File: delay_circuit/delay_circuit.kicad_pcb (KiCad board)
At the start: 2 copper layers, 97.5 x 139 mm, 26 parts, among them J1 IN 12V AC, J2 OUT 230V AC, J3 IN 230V AC, J4 From Trfo Output, J5 OUT 5V CC, J6 To Power Ampli Power IN, J7 From Ampli Output, J8 OUT 12V CC, J9 To Speakers, K1 SANYOU_SRD_Form_C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

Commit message: Fixed issues in source
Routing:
- net 0: track 0.42 -> 95.9 mm, vias 0 -> 2
- net Net-(D2-A): track 81.2 -> 82.9 mm
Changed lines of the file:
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@@
 		(legacy_teardrops no)
 	)
-	(paper "A4")
+	(paper "A4" portrait)
 	(layers
 		(0 "F.Cu" signal)
@@
 	)
 	(segment
+		(start 85 115)
+		(end 85 130)
+		(width 1.75)
+		(layer "F.Cu")
+		(net 3)
+	)
+	(via
+		(at 85 130)
+		(size 2.5)
+		(drill 0.8)
+		(layers "F.Cu" "B.Cu")
+		(net 3)
+	)
+	(via
+		(at 85 115)
+		(size 2.5)
+		(drill 0.8)
+		(layers "F.Cu" "B.Cu")
+		(net 3)
+	)
+	(segment
+		(start 107.5 125)
+		(end 103 129.5)
+		(width 1.75)
+		(layer "B.Cu")
+		(net 3)
+	)
+	(segment
+		(start 85 130)
+		(end 85 132.5)
+		(width 1.75)
+		(layer "B.Cu")
+		(net 3)
+	)
+	(segment
+		(start 103.294888 136)
+		(end 103.294888 129.794888)
+		(width 1.75)
+		(layer "B.Cu")
+		(net 3)
+	)
+	(segment
+		(start 102 96.88)
+		(end 102 107)
+		(width 1.75)
+		(layer "B.Cu")
+		(net 3)
+	)
+	(segment
+		(start 100 140)
+		(end 102.5 140)
+		(width 1.75)
+		(layer "B.Cu")
+		(net 3)
+	)
+	(segment
+		(start 102.5 140)
+		(end 103.294888 139.205112)
+		(width 1.75)
+		(layer "B.Cu")
+		(net 3)
+	)
+	(segment
 		(start 103.294888 129.794888)
 		(end 103 129.5)
@@
 	)
 	(segment
+		(start 95 135)
+		(end 100 140)
+		(width 1.75)
+		(layer "B.Cu")
+		(net 3)
+	)
+	(segment
+		(start 77.5775 108.5375)
+		(end 78.5375 108.5375)
+		(width 2)
+		(layer "B.Cu")
+		(net 3)
+	)
+	(segment
+		(start 85 132.5)
+		(end 87.5 135)
+		(width 1.75)
+		(layer "B.Cu")
+		(net 3)
+	)
+	(segment
+		(start 102 107)
+		(end 107.5 112.5)
+		(width 1.75)
+		(layer "B.Cu")
+		(net 3)
+	)
+	(segment
+		(start 107.5 112.5)
+		(end 107.5 125)
+		(width 1.75)
+		(layer "B.Cu")
+		(net 3)
+	)
+	(segment
+		(start 78.5375 108.5375)
+		(end 85 115)
+		(width 2)
+		(layer "B.Cu")
+		(net 3)
+	)
+	(segment
+		(start 103.294888 139.205112)
+		(end 103.294888 136)
+		(width 1.75)
+		(layer "B.Cu")
+		(net 3)
+	)
+	(segment
+		(start 87.5 135)
+		(end 95 135)
+		(width 1.75)
+		(layer "B.Cu")
+		(net 3)
+	)
+	(segment
 		(start 42 32)
 		(end 41.5 32.5)
@@
 	)
 	(segment
-		(start 56 102)
+		(start 55 102)
 		(end 63.5 102)
 		(width 2)
@@
 	)
 	(via
-		(at 56 102)
+		(at 55 102)
 		(size 2.5)
 		(drill 0.8)
@@
 	)
 	(segment
-		(start 49.5 102)
-		(end 56 102)
-		(width 1.2)
+		(start 68.25 101.75)
+		(end 71.5 105)
+		(width 2)
 		(layer "B.Cu")
 		(net 7)
@@
 		(start 67.55 96.05)
 		(end 67.55 100.95)
-		(width 1.2)
+		(width 2)
 		(layer "B.Cu")
 		(net 7)
@@
 	(segment
 		(start 47.05 99.45)
-		(end 47 99.5)
-		(width 1.2)
+		(end 47.05 96.05)
+		(width 2)
 		(layer "B.Cu")
 		(net 7)
@@
 		(start 68 102)
 		(end 68.25 101.75)
-		(width 1.2)
+		(width 2)
 		(layer "B.Cu")
 		(net 7)
@@
 	)
 	(segment
-		(start 99.58 88.4)
-		(end 91.1 96.88)
-		(width 1.2)
-		(layer "B.Cu")
-		(net 7)
-	)
-	(segment
 		(start 67.55 100.95)
 		(end 67.5 101)
@@
 		(start 67.5 101)
 		(end 68.25 101.75)
-		(width 1.2)
+		(width 2)
 		(layer "B.Cu")
 		(net 7)
@@
 		(start 89 107.5)
 		(end 89 103.5)
+		(width 2)
+		(layer "B.Cu")
+		(net 7)
+	)
+	(segment
+		(start 91.1 96.88)
+		(end 91.1 94.94)
 		(width 1.2)
 		(layer "B.Cu")
@@
 		(start 63.5 102)
 		(end 68 102)
-		(width 1.2)
+		(width 2)
 		(layer "B.Cu")
 		(net 7)
 	)
 	(segment
-		(start 69.5 103)
-		(end 88.5 103)
-		(width 1.2)
+		(start 49.5 102)
+		(end 47 99.5)
+		(width 2)
 		(layer "B.Cu")
 		(net 7)
 	)
 	(segment
-		(start 68.25 101.75)
-		(end 69.5 103)
-		(width 1.2)
+		(start 91.1 94.94)
+		(end 99.58 86.46)
+		(width 2)
 		(layer "B.Cu")
 		(net 7)
@@
 	)
 	(segment
-		(start 99.58 86.46)
-		(end 99.58 88.4)
+		(start 47 99.5)
+		(end 47.05 99.45)
 		(width 1.2)
 		(layer "B.Cu")
@@
 	)
 	(segment
-		(start 47 99.5)
+		(start 86.5 105)
+		(end 88.5 103)
+		(width 2)
+		(layer "B.Cu")
+		(net 7)
+	)
+	(segment
+		(start 55 102)
 		(end 49.5 102)
-		(width 1.2)
+		(width 2)
 		(layer "B.Cu")
 		(net 7)
@@
 		(start 89 100)
 		(end 91.1 97.9)
-		(width 1.2)
+		(width 2)
 		(layer "B.Cu")
 		(net 7)
 	)
 	(segment
-		(start 47.05 96.05)
-		(end 47.05 99.45)
-		(width 1.2)
+		(start 71.5 105)
+		(end 86.5 105)
+		(width 2)
 		(layer "B.Cu")
 		(net 7)
@@
 		(start 89 103.5)
 		(end 89 100)
-		(width 1.2)
+		(width 2)
 		(layer "B.Cu")
 		(net 7)
@@
 		(start 79.55 96.05)
 		(end 79.55 93.05)
-		(width 1.2)
+		(width 2)
 		(layer "B.Cu")
 		(net 8)
@@
 		(start 60.5375 123.5375)
 		(end 59 122)
-		(width 1.2)
+		(width 2)
 		(layer "B.Cu")
 		(net 8)
@@
 		(start 59.05 93.95)
 		(end 59.05 96.05)
-		(width 1.2)
+		(width 2)
 		(layer "B.Cu")
 		(net 8)
@@
 		(start 78.5 92)
 		(end 61 92)
-		(width 1.2)
+		(width 2)
 		(layer "B.Cu")
 		(net 8)
@@
 		(start 86.14 86.46)
 		(end 79.55 93.05)
-		(width 1.2)
+		(width 2)
 		(layer "B.Cu")
 		(net 8)
@@
 		(start 89.42 86.46)
 		(end 86.14 86.46)
-		(width 1.2)
+		(width 2)
 		(layer "B.Cu")
 		(net 8)
@@
 		(start 77.5775 123.5375)
 		(end 60.5375 123.5375)
-		(width 1.2)
+		(width 2)
 		(layer "B.Cu")
 		(net 8)
@@
 		(start 61 92)
 		(end 59.05 93.95)
-		(width 1.2)
+		(width 2)
 		(layer "B.Cu")
 		(net 8)
@@
 		(start 59.05 121.95)
 		(end 59.05 96.05)
-		(width 1.2)
+		(width 2)
 		(layer "B.Cu")
 		(net 8)
@@
 		(start 79.55 93.05)
 		(end 78.5 92)
-		(width 1.2)
+		(width 2)
 		(layer "B.Cu")
 		(net 8)
@@
 		(min_thickness 0.25)
 		(filled_areas_thickness no)
-		(fill yes
+		(fill
 			(thermal_gap 0.5)
 			(thermal_bridge_width 0.5)
@@
 		(min_thickness 0.25)
 		(filled_areas_thickness no)
-		(fill yes
+		(fill
 			(thermal_gap 0.5)
 			(thermal_bridge_width 0.5)
@@
 		(min_thickness 0.25)
 		(filled_areas_thickness no)
-		(fill yes
+		(fill
 			(thermal_gap 0.5)
 			(thermal_bridge_width 0.5)
@@
 		(min_thickness 0.25)
 		(filled_areas_thickness no)
-		(fill yes
+		(fill
 			(thermal_gap 0.5)
 			(thermal_bridge_width 0.5)
@@
 		(min_thickness 0.25)
 		(filled_areas_thickness no)
-		(fill yes
+		(fill
 			(thermal_gap 0.5)
 			(thermal_bridge_width 0.5)

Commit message: WIP
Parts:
- Q2: footprint Package_TO_SOT_THT:TO-3P-3_Vertical -> Package_TO_SOT_THT:TO-126-3_Vertical
- moved J5 10.1 mm to (95.0, 140.0), turned to -90 degrees
- moved Q2 9.52 mm to (92.7, 87.5)
- moved C1 7.00 mm to (73.8, 40.0)
- moved C2 7.00 mm to (62.8, 40.0)
- moved C3 7.00 mm to (100.5, 129.0)
- moved C4 7.00 mm to (41.2, 25.5)
- moved C5 7.00 mm to (62.8, 25.0)
- moved D1 7.00 mm to (42.8, 35.5)
- moved D2 7.00 mm to (89.2, 79.5)
- moved J1 7.00 mm to (28.0, 35.5)
- moved J2 7.00 mm to (27.2, 122.5)
- moved J3 7.00 mm to (27.2, 137.7)
- moved J4 7.00 mm to (27.8, 51.0)
- moved J6 7.00 mm to (27.8, 76.5)
- moved J7 7.00 mm to (27.2, 97.0)
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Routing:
- net Net-(J5-Pin_2): track 37.3 -> 43.8 mm
- net 0: track 95.9 -> 100.3 mm
- net Net-(J5-Pin_1): track 22.6 -> 18.8 mm
- net Net-(J7-Pin_4): track 110.3 -> 113.4 mm
- net Net-(Q1-E): track 21.1 -> 24.0 mm
- net OUT SP L+: track 75.0 -> 77.7 mm
- net OUT SP R+: track 72.0 -> 69.4 mm
- net 12V GND: track 150.9 -> 152.7 mm
- net Net-(D2-K): track 99.2 -> 100.5 mm
- net IN SP L+: track 71.5 -> 70.3 mm

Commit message: WIP
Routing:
- net 0: track 100.3 -> 105.3 mm
- net Net-(J2-Pin_2): track 73.8 -> 71.9 mm
- removed copper zone on B.Cu, net (none)
- removed copper zone on B.Cu, net 0
- removed copper zone on B.Cu, net 12V GND
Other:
- board size 97.5 x 139 mm -> 89.5 x 133 mm
- board text added: "+"
- board text added: "12V AC IN"
- board text added: "12V DC OUT"
- board text added: "230V AC"
- board text added: "5V DC OUT"
- board text added: "Ampli OUT"
- board text added: "POWER"
- board text added: "TR S1"
- board text added: "TR S2"
- board text added: "To Speakers"
- board text added: "© 2025"

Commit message: Updated board
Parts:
- moved J3 133.7 mm to (157.3, 106.6), turned to 0 degrees
- moved J5 120.0 mm to (159.5, 38.8), turned to 0 degrees
- moved J2 115.9 mm to (142.0, 106.6), turned to 0 degrees
- moved PS2 112.9 mm to (151.1, 86.1), turned to 90 degrees
- moved C3 107.1 mm to (148.5, 33.3), turned to 90 degrees
- moved R2 96.8 mm to (142.4, 38.1), turned to 180 degrees
- moved R1 94.6 mm to (142.4, 44.6), turned to 180 degrees
- moved J7 89.8 mm to (116.5, 106.6), turned to 0 degrees
- moved J8 84.6 mm to (43.0, 106.6), turned to 180 degrees
- moved PS1 80.6 mm to (126.1, 85.6), turned to 90 degrees
- moved R3 79.9 mm to (126.8, 31.1), turned to 0 degrees
- moved J1 75.4 mm to (55.0, 105.8), turned to 0 degrees
- moved J6 74.4 mm to (96.0, 106.1), turned to 0 degrees
- moved J4 69.7 mm to (70.5, 106.1), turned to 0 degrees
- moved C4 67.2 mm to (45.0, 92.6), turned to 180 degrees
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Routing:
- net 0: track 105.3 -> 107.4 mm
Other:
- board size 89.5 x 133 mm -> 133 x 90 mm

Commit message: Improved PCB.
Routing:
- net Net-(D2-K): track 100.1 -> 91.0 mm
- net OUT SP L+: track 77.7 -> 75.1 mm
- net Net-(J7-Pin_2): track 105.9 -> 104.4 mm
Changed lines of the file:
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@@
-	)
-	(segment
-		(start 136.0775 73.5425)
-		(end 134.54 75.08)
-		(width 2)
-		(layer "B.Cu")
-		(net 8)
 	)
 	(segment
 		(start 136.0775 56.5025)
-		(end 136.0775 50.9225)
+		(end 135.9975 56.5025)
 		(width 2)
 		(layer "B.Cu")
@@
 	)
 	(segment
-		(start 136.0775 50.9225)
+		(start 136.0775 56.5025)
+		(end 136.0775 49.4225)
+		(width 2)
+		(layer "B.Cu")
+		(net 8)
+	)
+	(segment
+		(start 140.92 44.58)
 		(end 142.42 44.58)
 		(width 2)
@@
 	)
 	(segment
-		(start 134.54 75.08)
-		(end 134.49 75.03)
-		(width 1.2)
-		(layer "B.Cu")
-		(net 8)
-	)
-	(segment
 		(start 99 44.66)
 		(end 99 50.79)
@@
 	)
 	(segment
+		(start 135.9975 56.5025)
+		(end 117.47 75.03)
+		(width 2)
+		(layer "B.Cu")
+		(net 8)
+	)
+	(segment
+		(start 117.47 75.03)
+		(end 108.59 75.03)
+		(width 2)
+		(layer "B.Cu")
+		(net 8)
+	)
+	(segment
 		(start 106.34 54.53)
 		(end 104.54 56.33)
@@
 	)
 	(segment
-		(start 136.0775 56.5025)
-		(end 136.0775 73.5425)
-		(width 2)
-		(layer "B.Cu")
-		(net 8)
-	)
-	(segment
-		(start 134.49 75.03)
-		(end 108.59 75.03)
+		(start 136.0775 49.4225)
+		(end 140.92 44.58)
 		(width 2)
 		(layer "B.Cu")
@@
 	)
 	(segment
+		(start 105.54 87.04)
+		(end 100.58 82.08)
+		(width 2.5)
+		(layer "B.Cu")
+		(net 17)
+	)
+	(segment
+		(start 100.58 82.08)
+		(end 87.29 82.08)
+		(width 2.5)
+		(layer "B.Cu")
+		(net 17)
+	)
+	(segment
+		(start 117.04 91.33)
+		(end 107.79 91.33)
+		(width 2.5)
+		(layer "B.Cu")
+		(net 17)
+	)
+	(segment
+		(start 117.04 101.33)
+		(end 117.04 91.33)
+		(width 2.5)
+		(layer "B.Cu")
+		(net 17)
+	)
+	(segment
+		(start 121.54 105.83)
+		(end 117.04 101.33)
+		(width 2.5)
+		(layer "B.Cu")
+		(net 17)
+	)
+	(segment
 		(start 87.29 82.08)
 		(end 69.04 63.83)
@@
 	)
 	(segment
-		(start 105.54 89.08)
-		(end 105.54 84.58)
-		(width 2.5)
-		(layer "B.Cu")
-		(net 17)
-	)
-	(segment
 		(start 121.54 106.58)
 		(end 121.54 105.83)
@@
 	)
 	(segment
-		(start 105.54 84.58)
-		(end 103.04 82.08)
-		(width 2.5)
-		(layer "B.Cu")
-		(net 17)
-	)
-	(segment
-		(start 103.04 82.08)
-		(end 87.29 82.08)
-		(width 2.5)
-		(layer "B.Cu")
-		(net 17)
-	)
-	(segment
-		(start 117.04 101.33)
-		(end 117.04 91.33)
-		(width 2.5)
-		(layer "B.Cu")
-		(net 17)
-	)
-	(segment
-		(start 117.04 91.33)
-		(end 107.79 91.33)
-		(width 2.5)
-		(layer "B.Cu")
-		(net 17)
-	)
-	(segment
-		(start 121.54 105.83)
-		(end 117.04 101.33)
+		(start 107.79 91.33)
+		(end 105.54 89.08)
+		(width 2.5)
+		(layer "B.Cu")
+		(net 17)
+	)
+	(segment
+		(start 105.54 89.08)
+		(end 105.54 87.04)
 		(width 2.5)
 		(layer "B.Cu")
@@
 	)
 	(segment
-		(start 107.79 91.33)
-		(end 105.54 89.08)
-		(width 2.5)
-		(layer "B.Cu")
-		(net 17)
-	)
-	(segment
 		(start 122.04 93.58)
 		(end 96.54 93.58)
@@
 	)
 	(segment
+		(start 92.04 48.83)
+		(end 92.04 42.54)
+		(width 2.5)
+		(layer "B.Cu")
+		(net 20)
+	)
+	(segment
 		(start 110.54 60.58)
 		(end 111.54 60.58)
@@
 	)
 	(segment
+		(start 81.58 32.08)
+		(end 66.54 32.08)
+		(width 2.5)
+		(layer "B.Cu")
+		(net 20)
+	)
+	(segment
 		(start 112.54 51.08)
 		(end 110.04 48.58)
@@
 	)
 	(segment
-		(start 86.04 32.08)
-		(end 66.54 32.08)
-		(width 2.5)
-		(layer "B.Cu")
-		(net 20)
-	)
-	(segment
-		(start 92.04 48.83)
-		(end 92.04 38.08)
+		(start 64.04 34.58)
+		(end 64.04 37.08)
+		(width 2.5)
+		(layer "B.Cu")
+		(net 20)
+	)
+	(segment
+		(start 92.04 42.54)
+		(end 81.58 32.08)
+		(width 2.5)
+		(layer "B.Cu")
+		(net 20)
+	)
+	(segment
+		(start 110.04 48.58)
+		(end 103.54 48.58)
 		(width 2.5)
 		(layer "B.Cu")
@@
 	)
 	(segment
-		(start 110.04 48.58)
-		(end 103.54 48.58)
-		(width 2.5)
-		(layer "B.Cu")
-		(net 20)
-	)
-	(segment
 		(start 113.04 51.58)
 		(end 112.54 51.08)
 		(width 2.5)
 		(layer "B.Cu")
-		(net 20)
-	)
-	(segment
-		(start 92.04 38.08)
-		(end 86.04 32.08)
-		(width 2.5)
-		(layer "B.Cu")
-		(net 20)
-	)
-	(segment
-		(start 64.04 34.58)
-		(end 64.04 37.08)
-		(width 2.5)
-		(layer "B.Cu")

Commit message: Improved board.
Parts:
- PS1, PS2: footprint Converter_ACDC:Converter_ACDC_Hi-Link_HLK-PMxx -> Components:Converter_ACDC_Hi-Link_HLK-PMxx
- Q2: footprint Package_TO_SOT_THT:TO-126-3_Vertical -> Components:TO-126-3_Vertical
- R1, R2, R3: footprint Resistor_THT:R_Axial_DIN0411_L9.9mm_D3.6mm_P15.24mm_Horizontal -> Resistor_THT:R_Axial_DIN0207_L6.3mm_D2.5mm_P15.24mm_Horizontal
- moved C1 26.3 mm to (55.0, 86.0)
- moved K1 22.3 mm to (89.0, 66.5), turned to -90 degrees
- moved D2 21.7 mm to (116.5, 57.5), turned to 180 degrees
- moved C3 19.5 mm to (144.0, 52.2)
- moved J9 17.7 mm to (90.0, 51.0)
- moved C5 16.9 mm to (44.5, 88.0), turned to 180 degrees
- moved U1 16.4 mm to (48.5, 62.5)
- moved R3 16.2 mm to (121.9, 46.5)
- moved K2 15.3 mm to (107.5, 66.0), turned to -90 degrees
- moved R2 14.0 mm to (137.1, 51.0)
- moved J5 13.1 mm to (154.8, 51.0)
- moved R1 12.6 mm to (137.1, 56.0)
- moved Q1 11.1 mm to (117.5, 53.5)
- moved Q2 7.53 mm to (108.5, 48.5), turned to -90 degrees
- moved C2 7.35 mm to (55.2, 77.0)
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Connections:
- K1 pad 3: unconnected-(K1-Pad3) -> IN SP L+
- K1 pad 4: IN SP L+ -> unconnected-(K1-Pad4)
- K2 pad 3: unconnected-(K2-Pad3) -> IN SP R+
- K2 pad 4: IN SP R+ -> unconnected-(K2-Pad4)
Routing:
- net 12V GND: track 152.7 -> 97.7 mm
- net OUT SP L+: track 75.1 -> 29.6 mm
- net Net-(D2-A): track 83.1 -> 48.6 mm, vias 2 -> 0
- net OUT SP R+: track 69.4 -> 42.2 mm, vias 0 -> 2
- net IN SP L+: track 70.3 -> 48.7 mm, vias 2 -> 0
- net Net-(J7-Pin_2): track 104.4 -> 83.9 mm
- net Net-(J8-Pin_1): track 78.0 -> 57.6 mm
- net Net-(J5-Pin_2): track 43.8 -> 26.3 mm
- net 0: track 107.4 -> 91.3 mm, vias 2 -> 0
- net Net-(D1-+): track 54.4 -> 39.4 mm
- net Net-(J2-Pin_2): track 71.9 -> 59.2 mm
- net Net-(J7-Pin_4): track 113.4 -> 124.7 mm, vias 4 -> 2
- net Net-(Q1-E): track 24.0 -> 14.2 mm
- net Net-(D2-K): track 91.0 -> 82.4 mm
- net Net-(J1-Pin_1): track 23.1 -> 17.0 mm
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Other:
- board size 133 x 90 mm -> 133 x 71 mm
- board text removed: "12V AC IN"
- board text removed: "12V DC OUT"
- board text removed: "230V AC"
- board text removed: "5V DC OUT"
- board text removed: "Ampli OUT"
- board text removed: "POWER"
- board text removed: "TR S1"
- board text removed: "TR S2"
- board text removed: "To Speakers"
- board text removed: "© 2025"

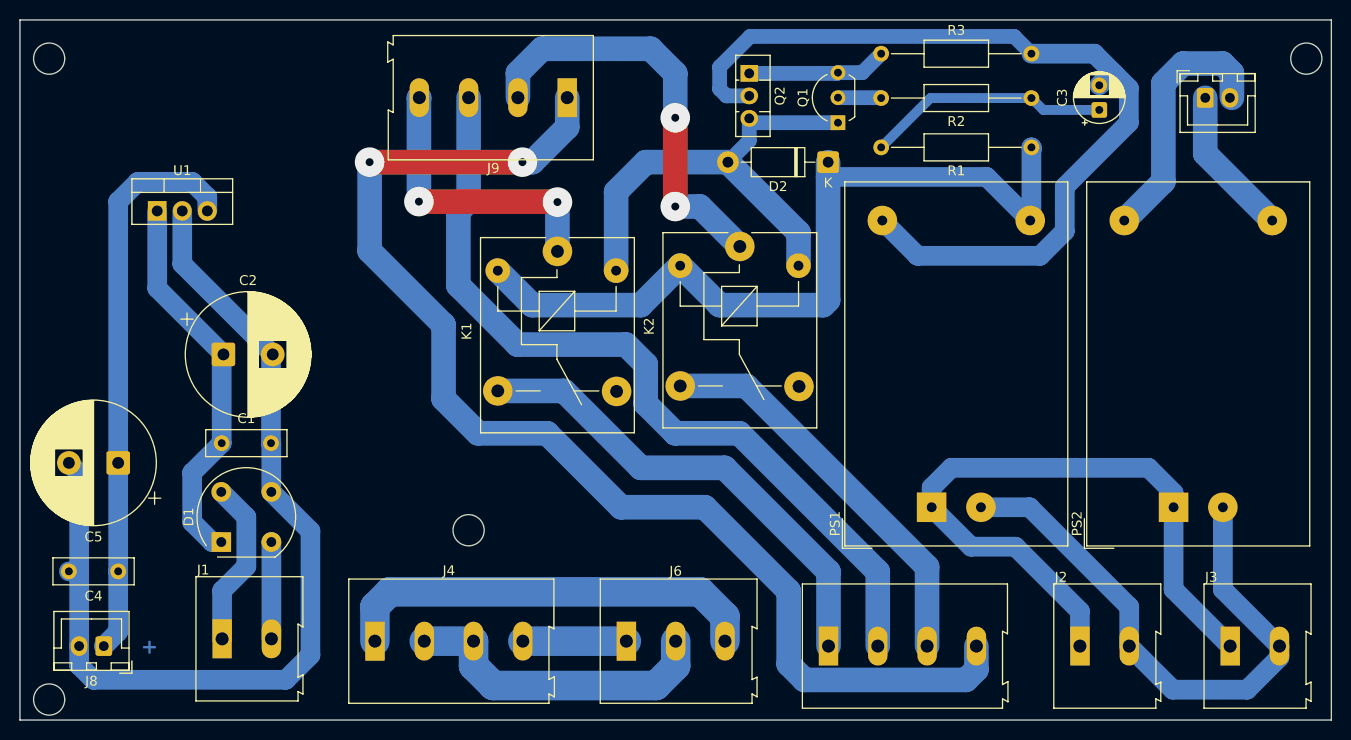
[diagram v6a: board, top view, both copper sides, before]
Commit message: Reduced board size.
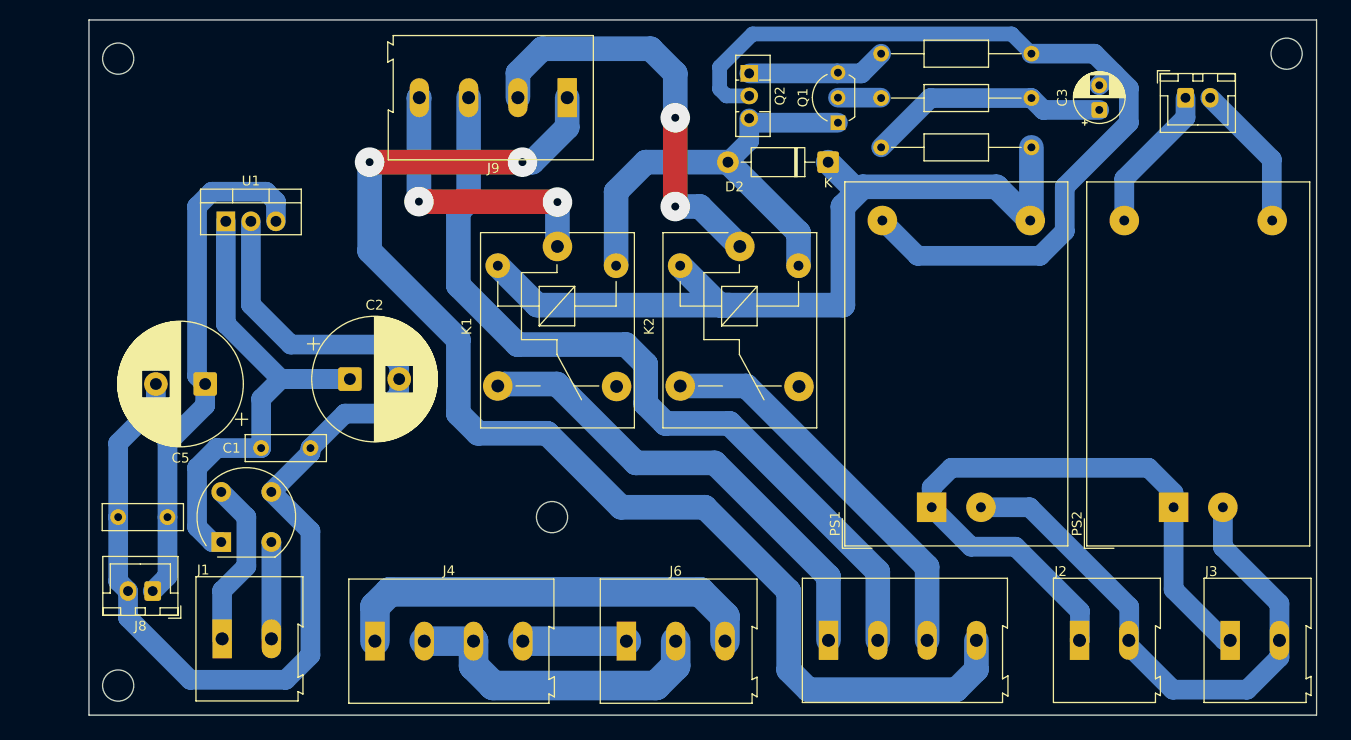
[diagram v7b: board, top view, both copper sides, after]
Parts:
- moved C2 13.1 mm to (68.0, 79.5)
- moved C5 11.9 mm to (53.3, 80.0)
- moved J8 7.47 mm to (48.0, 101.0)
- moved C4 7.43 mm to (49.5, 93.5)
- moved U1 7.04 mm to (55.4, 63.5)
- moved C1 4.03 mm to (59.0, 86.5)
- moved J5 2.00 mm to (152.8, 51.0)
- moved J2 0.58 mm to (142.0, 106.0)
- moved J3 0.58 mm to (157.3, 106.0)
- moved J7 0.58 mm to (116.5, 106.0)
- moved K1 0.50 mm to (89.0, 66.0)
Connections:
- PS2 pad 3: Net-(J5-Pin_2) -> Net-(J5-Pin_1)
- PS2 pad 4: Net-(J5-Pin_1) -> Net-(J5-Pin_2)
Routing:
- net Net-(D1-+): track 39.4 -> 56.1 mm
- net 12V GND: track 97.7 -> 112.5 mm
- net Net-(J5-Pin_2): track 26.3 -> 15.1 mm
- net Net-(J8-Pin_1): track 57.6 -> 52.6 mm
- net Net-(D2-K): track 82.4 -> 86.7 mm
- net Net-(J7-Pin_4): track 124.7 -> 126.4 mm
- net Net-(J2-Pin_1): track 69.3 -> 68.5 mm
- net Net-(J7-Pin_2): track 83.9 -> 83.3 mm
- net IN SP R+: track 40.7 -> 40.1 mm
- net IN SP L+: track 48.7 -> 48.2 mm
- net OUT SP L+: track 29.6 -> 29.1 mm
- net Net-(D2-A): track 48.6 -> 48.1 mm
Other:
- board size 133 x 71 mm -> 124.5 x 70.5 mm
- board text removed: "+"
